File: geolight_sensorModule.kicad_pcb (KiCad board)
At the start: 2 copper layers, 20 parts, among them IC1 ATTINY841-SSU, P1 5V, P2 ICSP, P3 IN, P4 OUT, P5 OUT (JP for IN), P6 UART(test), U1 TCRT5000/L, Y1 16Mhz

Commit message: removed 3rd, reversible jumper connector (difficult to mirror if reversible, probably not necessary to have 3)
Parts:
- removed JP1: IN/OUT, Connect:GS3
- removed P5: OUT (JP for IN), Pin_Headers:Pin_Header_Angled_1x06
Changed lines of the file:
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@@
 (kicad_pcb (version 4) (host pcbnew 4.0.2-stable)
   (general
-    (links 55)
-    (no_connects 55)
-    (area 103.261238 85.753 196.168001 165.4908)
+    (links 46)
+    (no_connects 46)
+    (area 0 0 0 0)
     (thickness 1.6)
     (drawings 0)
     (tracks 0)
     (zones 0)
-    (modules 20)
+    (modules 18)
     (nets 18)
   )
@@
       (rotate (xyz 0 0 0))
     )
-  )
-  (module Connect:GS3 (layer F.Cu)
-    (at 176.657 154.94)
-    (descr "Pontet Goute de soudure")
-    (attr virtual)
-    (fp_text reference JP1 (at 1.524 0 90) (layer F.SilkS)
-      (effects (font (size 1 1) (thickness 0.15)))
-    )
-    (fp_text value IN/OUT (at 1.524 0 90) (layer F.Fab)
-      (effects (font (size 1 1) (thickness 0.15)))
-    )
-    (fp_line (start -0.889 -1.905) (end -0.889 1.905) (layer F.SilkS) (width 0.15))
-    (fp_line (start -0.889 1.905) (end 0.889 1.905) (layer F.SilkS) (width 0.15))
-    (fp_line (start 0.889 1.905) (end 0.889 -1.905) (layer F.SilkS) (width 0.15))
-    (fp_line (start -0.889 -1.905) (end 0.889 -1.905) (layer F.SilkS) (width 0.15))
-    (pad 1 smd rect (at 0 -1.27) (size 1.27 0.9652) (layers F.Cu F.Paste F.Mask)
-      (net 10 /MISO))
-    (pad 2 smd rect (at 0 0) (size 1.27 0.9652) (layers F.Cu F.Paste F.Mask)
-      (net 10 /MISO))
-    (pad 3 smd rect (at 0 1.27) (size 1.27 0.9652) (layers F.Cu F.Paste F.Mask)
-      (net 9 /SDA/MOSI))
   )
   (module Terminal_Blocks:TerminalBlock_Pheonix_MPT-2.54mm_2pol (layer F.Cu)
@@
       (effects (font (size 1 1) (thickness 0.15)))
     )
-    (fp_line (start -1.5 -1.75) (end -1.5 14.45) (layer F.CrtYd) (width 0.05))
-    (fp_line (start 10.65 -1.75) (end 10.65 14.45) (layer F.CrtYd) (width 0.05))
-    (fp_line (start -1.5 -1.75) (end 10.65 -1.75) (layer F.CrtYd) (width 0.05))
-    (fp_line (start -1.5 14.45) (end 10.65 14.45) (layer F.CrtYd) (width 0.05))
-    (fp_line (start -1.3 -1.55) (end -1.3 0) (layer F.SilkS) (width 0.15))
-    (fp_line (start 0 -1.55) (end -1.3 -1.55) (layer F.SilkS) (width 0.15))
-    (fp_line (start 4.191 -0.127) (end 10.033 -0.127) (layer F.SilkS) (width 0.15))
-    (fp_line (start 10.033 -0.127) (end 10.033 0.127) (layer F.SilkS) (width 0.15))
-    (fp_line (start 10.033 0.127) (end 4.191 0.127) (layer F.SilkS) (width 0.15))
-    (fp_line (start 4.191 0.127) (end 4.191 0) (layer F.SilkS) (width 0.15))
-    (fp_line (start 4.191 0) (end 10.033 0) (layer F.SilkS) (width 0.15))
-    (fp_line (start 1.524 -0.254) (end 1.143 -0.254) (layer F.SilkS) (width 0.15))
-    (fp_line (start 1.524 0.254) (end 1.143 0.254) (layer F.SilkS) (width 0.15))
-    (fp_line (start 1.524 2.286) (end 1.143 2.286) (layer F.SilkS) (width 0.15))
-    (fp_line (start 1.524 2.794) (end 1.143 2.794) (layer F.SilkS) (width 0.15))
-    (fp_line (start 1.524 4.826) (end 1.143 4.826) (layer F.SilkS) (width 0.15))
-    (fp_line (start 1.524 5.334) (end 1.143 5.334) (layer F.SilkS) (width 0.15))
-    (fp_line (start 1.524 12.954) (end 1.143 12.954) (layer F.SilkS) (width 0.15))
-    (fp_line (start 1.524 12.446) (end 1.143 12.446) (layer F.SilkS) (width 0.15))
-    (fp_line (start 1.524 10.414) (end 1.143 10.414) (layer F.SilkS) (width 0.15))
-    (fp_line (start 1.524 9.906) (end 1.143 9.906) (layer F.SilkS) (width 0.15))
-    (fp_line (start 1.524 7.874) (end 1.143 7.874) (layer F.SilkS) (width 0.15))
-    (fp_line (start 1.524 7.366) (end 1.143 7.366) (layer F.SilkS) (width 0.15))
-    (fp_line (start 1.524 -1.27) (end 4.064 -1.27) (layer F.SilkS) (width 0.15))
-    (fp_line (start 1.524 1.27) (end 4.064 1.27) (layer F.SilkS) (width 0.15))
-    (fp_line (start 1.524 1.27) (end 1.524 3.81) (layer F.SilkS) (width 0.15))
-    (fp_line (start 1.524 3.81) (end 4.064 3.81) (layer F.SilkS) (width 0.15))
-    (fp_line (start 4.064 2.286) (end 10.16 2.286) (layer F.SilkS) (width 0.15))
-    (fp_line (start 10.16 2.286) (end 10.16 2.794) (layer F.SilkS) (width 0.15))
-    (fp_line (start 10.16 2.794) (end 4.064 2.794) (layer F.SilkS) (width 0.15))
-    (fp_line (start 4.064 3.81) (end 4.064 1.27) (layer F.SilkS) (width 0.15))
-    (fp_line (start 4.064 1.27) (end 4.064 -1.27) (layer F.SilkS) (width 0.15))
-    (fp_line (start 10.16 0.254) (end 4.064 0.254) (layer F.SilkS) (width 0.15))
-    (fp_line (start 10.16 -0.254) (end 10.16 0.254) (layer F.SilkS) (width 0.15))
-    (fp_line (start 4.064 -0.254) (end 10.16 -0.254) (layer F.SilkS) (width 0.15))
-    (fp_line (start 1.524 1.27) (end 4.064 1.27) (layer F.SilkS) (width 0.15))
-    (fp_line (start 1.524 -1.27) (end 1.524 1.27) (layer F.SilkS) (width 0.15))
-    (fp_line (start 1.524 8.89) (end 4.064 8.89) (layer F.SilkS) (width 0.15))
-    (fp_line (start 1.524 8.89) (end 1.524 11.43) (layer F.SilkS) (width 0.15))
-    (fp_line (start 1.524 11.43) (end 4.064 11.43) (layer F.SilkS) (width 0.15))
-    (fp_line (start 4.064 9.906) (end 10.16 9.906) (layer F.SilkS) (width 0.15))
-    (fp_line (start 10.16 9.906) (end 10.16 10.414) (layer F.SilkS) (width 0.15))
-    (fp_line (start 10.16 10.414) (end 4.064 10.414) (layer F.SilkS) (width 0.15))
-    (fp_line (start 4.064 11.43) (end 4.064 8.89) (layer F.SilkS) (width 0.15))
-    (fp_line (start 4.064 13.97) (end 4.064 11.43) (layer F.SilkS) (width 0.15))
-    (fp_line (start 10.16 12.954) (end 4.064 12.954) (layer F.SilkS) (width 0.15))
-    (fp_line (start 10.16 12.446) (end 10.16 12.954) (layer F.SilkS) (width 0.15))
-    (fp_line (start 4.064 12.446) (end 10.16 12.446) (layer F.SilkS) (width 0.15))
-    (fp_line (start 1.524 13.97) (end 4.064 13.97) (layer F.SilkS) (width 0.15))
-    (fp_line (start 1.524 11.43) (end 1.524 13.97) (layer F.SilkS) (width 0.15))
-    (fp_line (start 1.524 11.43) (end 4.064 11.43) (layer F.SilkS) (width 0.15))
-    (fp_line (start 1.524 6.35) (end 4.064 6.35) (layer F.SilkS) (width 0.15))
-    (fp_line (start 1.524 6.35) (end 1.524 8.89) (layer F.SilkS) (width 0.15))
-    (fp_line (start 1.524 8.89) (end 4.064 8.89) (layer F.SilkS) (width 0.15))
-    (fp_line (start 4.064 7.366) (end 10.16 7.366) (layer F.SilkS) (width 0.15))
-    (fp_line (start 10.16 7.366) (end 10.16 7.874) (layer F.SilkS) (width 0.15))
-    (fp_line (start 10.16 7.874) (end 4.064 7.874) (layer F.SilkS) (width 0.15))
-    (fp_line (start 4.064 8.89) (end 4.064 6.35) (layer F.SilkS) (width 0.15))
-    (fp_line (start 4.064 6.35) (end 4.064 3.81) (layer F.SilkS) (width 0.15))
-    (fp_line (start 10.16 5.334) (end 4.064 5.334) (layer F.SilkS) (width 0.15))
-    (fp_line (start 10.16 4.826) (end 10.16 5.334) (layer F.SilkS) (width 0.15))
-    (fp_line (start 4.064 4.826) (end 10.16 4.826) (layer F.SilkS) (width 0.15))
-    (fp_line (start 1.524 6.35) (end 4.064 6.35) (layer F.SilkS) (width 0.15))
-    (fp_line (start 1.524 3.81) (end 1.524 6.35) (layer F.SilkS) (width 0.15))
-    (fp_line (start 1.524 3.81) (end 4.064 3.81) (layer F.SilkS) (width 0.15))
-    (pad 1 thru_hole rect (at 0 0) (size 2.032 1.7272) (drill 1.016) (layers *.Cu *.Mask F.SilkS)
-      (net 1 +5V))
-    (pad 2 thru_hole oval (at 0 2.54) (size 2.032 1.7272) (drill 1.016) (layers *.Cu *.Mask F.SilkS)
-      (net 2 GND))
-    (pad 3 thru_hole oval (at 0 5.08) (size 2.032 1.7272) (drill 1.016) (layers *.Cu *.Mask F.SilkS)
-      (net 11 /SCK/SCL))
-    (pad 4 thru_hole oval (at 0 7.62) (size 2.032 1.7272) (drill 1.016) (layers *.Cu *.Mask F.SilkS)
-      (net 10 /MISO))
-    (pad 5 thru_hole oval (at 0 10.16) (size 2.032 1.7272) (drill 1.016) (layers *.Cu *.Mask F.SilkS)
-      (net 9 /SDA/MOSI))
-    (pad 6 thru_hole oval (at 0 12.7) (size 2.032 1.7272) (drill 1.016) (layers *.Cu *.Mask F.SilkS)
-      (net 8 /SS))
-    (model Pin_Headers.3dshapes/Pin_Header_Angled_1x06.wrl
-      (at (xyz 0 -0.25 0))
-      (scale (xyz 1 1 1))
-      (rotate (xyz 0 0 90))
-    )
-  )
-  (module Pin_Headers:Pin_Header_Angled_1x06 (layer F.Cu)
-    (at 185.293 137.287)
-    (descr "Through hole pin header")
-    (tags "pin header")
-    (fp_text reference P5 (at 0 -5.1) (layer F.SilkS)
-      (effects (font (size 1 1) (thickness 0.15)))
-    )
-    (fp_text value "OUT (JP for IN)" (at 0 -3.1) (layer F.Fab)
-      (effects (font (size 1 1) (thickness 0.15)))
-    )

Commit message: fixed mirrored in/out. updated netlist, footprints, PCB. Fixed UART test point rats nest
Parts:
- removed R2, R3: 4k7, Discret:R1
- added JP1: I2C/SS, Connect:GS3, F.Cu at (190.8, 120.0)
- added JP2: MISO EN, Connect:GS2, F.Cu at (193.4, 121.3)
- P3, P4: footprint Pin_Headers:Pin_Header_Angled_1x06 -> Pin_Headers:Pin_Header_Straight_1x06
- moved IC1 61.9 mm to (157.6, 149.6)
- moved P6 34.5 mm to (174.8, 152.4), turned to 90 degrees
- moved P3 23.2 mm to (122.3, 131.1)
- moved P4 18.1 mm to (197.4, 128.9), turned to 180 degrees
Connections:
- P4 pad 4: /MISO -> Net-(JP2-Pad1)

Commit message: minor changes.
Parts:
- added P5: AUX_SENSOR, Pin_Headers:Pin_Header_Straight_1x03, F.Cu at (185.5, 114.3)
- IC1: value ATTINY841-SSU -> ATTINY841
- P6: value UART(test) -> UART
- moved C2 40.5 mm to (158.0, 139.6), turned to 180 degrees
- moved C1 37.2 mm to (168.1, 127.1)
- moved C3 34.4 mm to (148.8, 120.8), turned to 180 degrees
- moved JP1 29.9 mm to (163.4, 132.2), turned to 0 degrees
- moved JP2 29.5 mm to (165.6, 131.2)
- moved P6 28.0 mm to (153.0, 134.7), turned to 270 degrees
- moved Y1 26.3 mm to (163.3, 136.5), turned to 90 degrees
- moved P1 24.7 mm to (170.6, 120.8), turned to 180 degrees
- moved P4 22.5 mm to (174.9, 128.7), turned to 330 degrees
- moved R6 19.5 mm to (154.3, 120.5)
- moved P3 19.3 mm to (141.5, 128.6), turned to 30 degrees
- moved IC1 15.6 mm to (158.0, 134.0), turned to 180 degrees
- moved P2 13.7 mm to (150.1, 130.6), turned to 180 degrees
- moved R4 9.74 mm to (161.3, 120.5)
- moved R5 9.43 mm to (162.1, 117.1)
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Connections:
- IC1 pad 10: Net-(IC1-Pad10) -> /AUX

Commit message: re-arranged PCB, routing done (all except ground plane)
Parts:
- D1, U1: moved to B.Cu
- IC1: value ATTINY841 -> ATTINY841-SSU
- JP2: footprint Connect:GS2 -> Connect:GS3
- moved C2 27.8 mm to (145.0, 114.9), turned to 90 degrees
- moved P6 25.1 mm to (149.6, 109.9), turned to 180 degrees
- moved Y1 21.8 mm to (148.9, 120.1), turned to 0 degrees
- moved IC1 20.6 mm to (150.2, 114.9), turned to 90 degrees
- moved P5 18.2 mm to (167.4, 113.7)
- moved C3 12.0 mm to (157.5, 112.5), turned to 90 degrees
- moved C1 10.9 mm to (161.7, 118.4)
- moved R4 10.7 mm to (150.8, 122.6), turned to 180 degrees
- moved P1 10.5 mm to (164.2, 112.4)
- moved P4 9.52 mm to (171.4, 119.8)
- moved P3 9.04 mm to (143.5, 119.8)
- moved JP2 8.26 mm to (165.9, 122.9), turned to 180 degrees
- moved JP1 8.02 mm to (164.0, 124.2)
- moved R1 7.50 mm to (162.1, 126.7), turned to 90 degrees
- moved R6 5.58 mm to (152.7, 125.9), turned to 270 degrees
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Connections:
- IC1 pad 4: Net-(IC1-Pad4) -> /RESET
- R4 pad 2: Net-(IC1-Pad4) -> /RESET
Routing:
- net +5V: track 0.00 -> 62.6 mm, vias 0 -> 1
- net /SCK/SCL: track 0.00 -> 55.8 mm
- net /MISO: track 0.00 -> 50.5 mm, vias 0 -> 2
- net /SDA/MOSI: track 0.00 -> 49.7 mm
- net /SS: track 0.00 -> 33.5 mm, vias 0 -> 2
- net /RESET: track 0.00 -> 20.8 mm
- net Net-(IC1-Pad13): track 0.00 -> 19.3 mm, vias 0 -> 2
- net /AUX: track 0.00 -> 19.2 mm
- net Net-(IC1-Pad5): track 0.00 -> 16.0 mm
- net Net-(JP2-Pad1): track 0.00 -> 3.03 mm
- net Net-(IC1-Pad3): track 0.00 -> 3.01 mm
- net /TX: track 0.00 -> 2.61 mm
- net /RX: track 0.00 -> 2.61 mm
- net Net-(IC1-Pad2): track 0.00 -> 2.55 mm
- net Net-(R1-Pad2): track 0.00 -> 2.20 mm
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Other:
- board outline added: 33 x 24.9 mm

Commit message: finished v0.99 (no top copper pour)
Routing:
- net GND: track 0.00 -> 82.8 mm, vias 0 -> 3
- net +5V: track 62.6 -> 77.4 mm, vias 1 -> 5
- net /SDA/MOSI: track 49.7 -> 52.1 mm
- net Net-(IC1-Pad5): track 16.0 -> 17.6 mm
- net Net-(IC1-Pad13): track 19.3 -> 20.7 mm
- net /RESET: track 20.8 -> 22.2 mm
- net /SCK/SCL: track 55.8 -> 56.6 mm
- net /MISO: track 50.5 -> 49.7 mm
- net /SS: track 33.5 -> 33.9 mm, vias 2 -> 4
- added copper zone on B.Cu, net GND

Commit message: v1.0! added top layer
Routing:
- net GND: track 82.8 -> 174.8 mm, vias 3 -> 30
- added copper zone on F.Cu, net GND

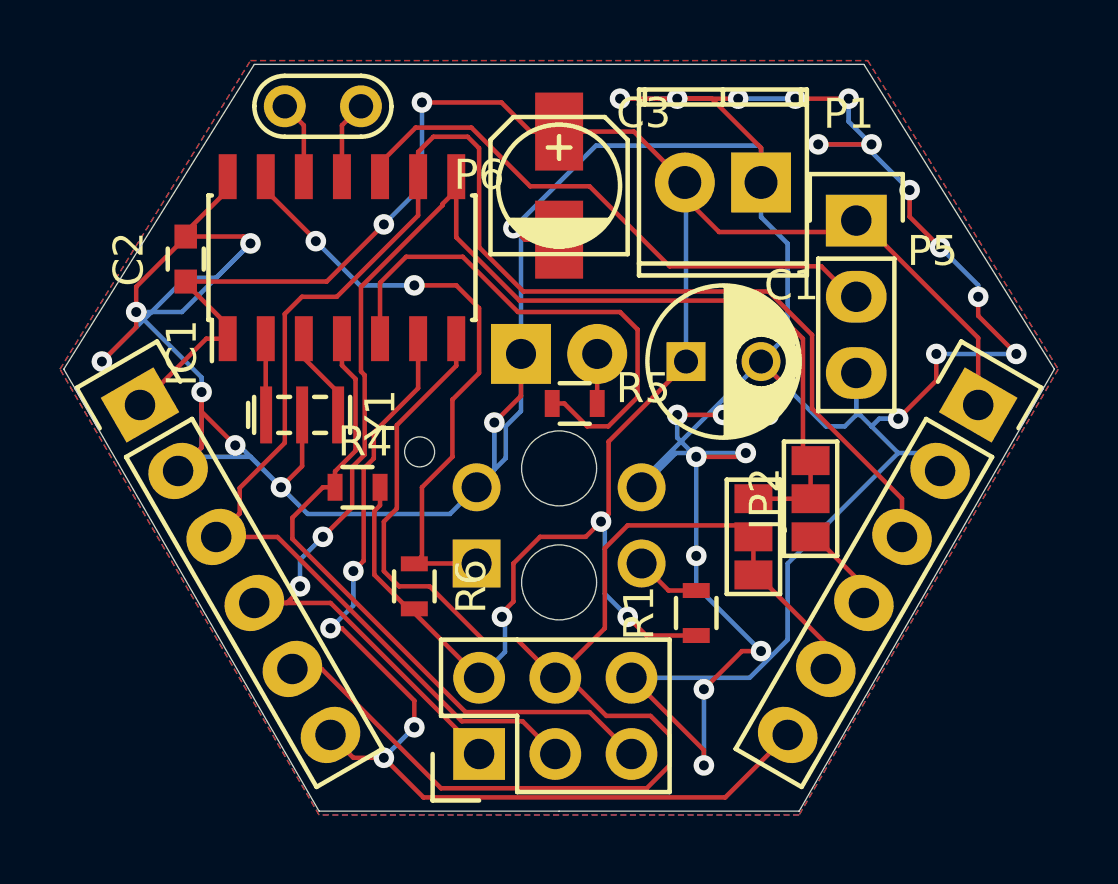
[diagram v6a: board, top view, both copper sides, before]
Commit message: silkscreen changes
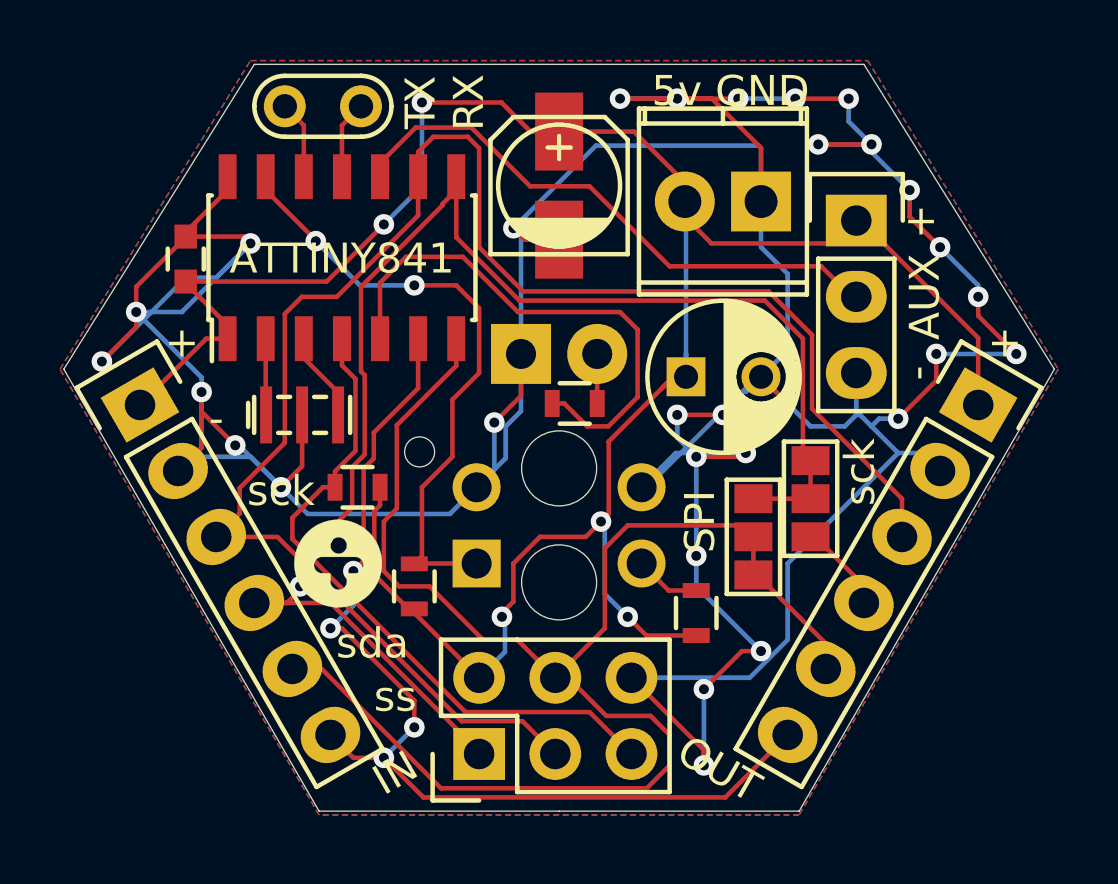
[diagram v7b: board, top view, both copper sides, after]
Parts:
- added G***: LOGO, Symbols:TI_Logo_F.SilkS_3mm, F.Cu at (150.1, 125.1)
- moved 5V 0.64 mm to (164.2, 113.0)
- moved C1 0.51 mm to (161.7, 118.9)
- renumbered Y1 to 16M, P1 to 5V, IC1 to ATTINY841, P5 to AUX, P3 to IN, P4 to OUT, JP2 to SPI, P6 to tx/rx
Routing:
- net +5V: track 77.4 -> 79.8 mm
- net GND: track 174.8 -> 176.4 mm
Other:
- board text added: "+"
- board text added: "-"
- board text added: "5v GND"
- board text added: "TX RX"
- board text added: "sck"
- board text added: "sda"
- board text added: "ss"

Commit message: RELEASE rev 1.0 (sent to elecrow)
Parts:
- added G***: LOGO, Symbols:TI_Logo_F.SilkS_15mm, B.Cu at (149.6, 119.3)
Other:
- board text added: "V1.0"
- board text added: "geodome rev 1.0"
